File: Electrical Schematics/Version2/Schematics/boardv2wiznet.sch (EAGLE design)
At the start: 19 parts

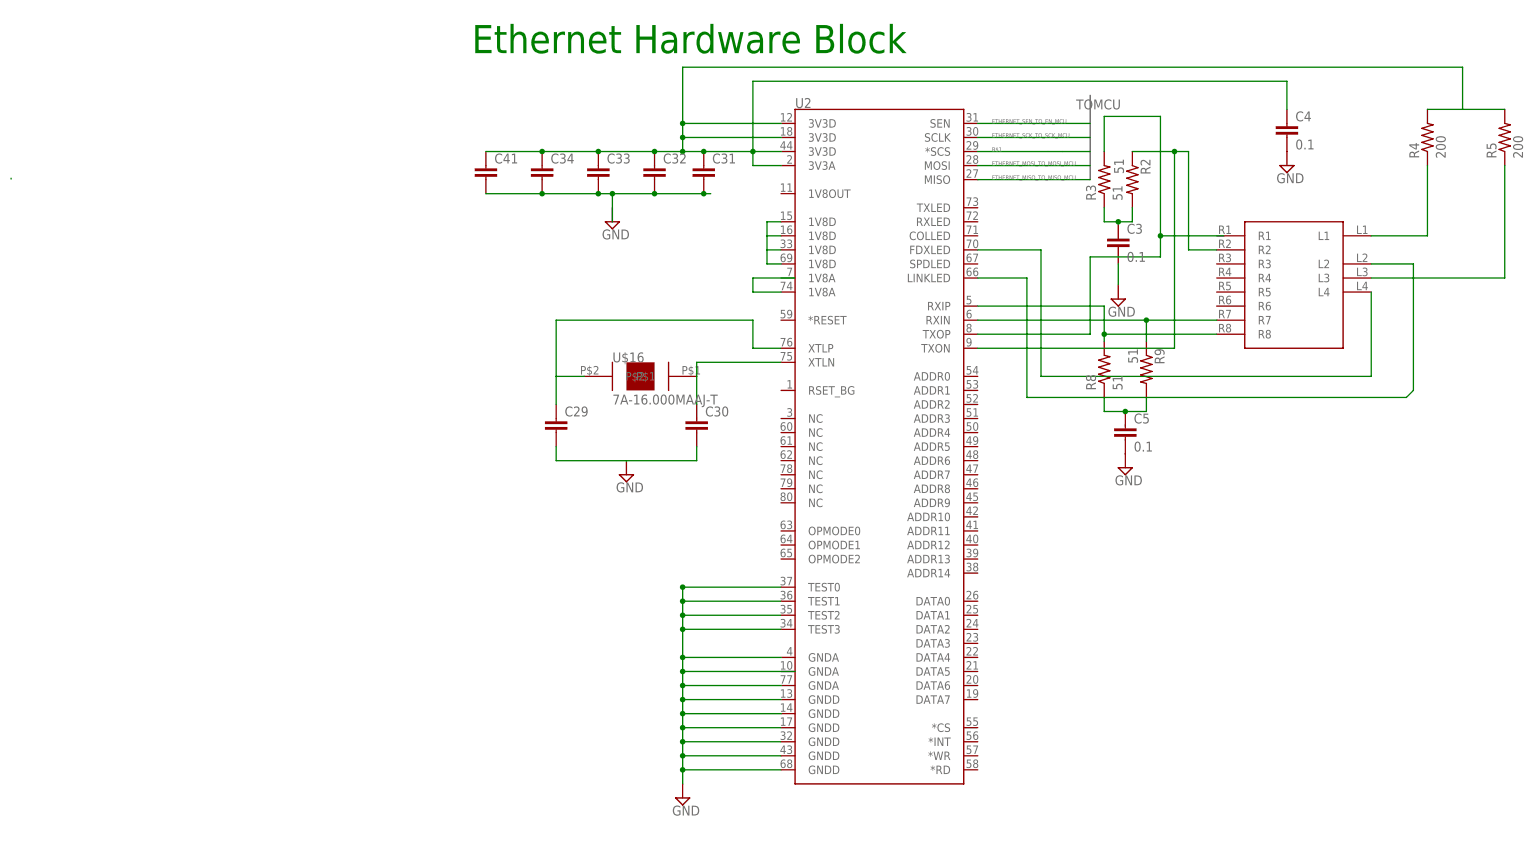
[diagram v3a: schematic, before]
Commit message: updated power and ethernet
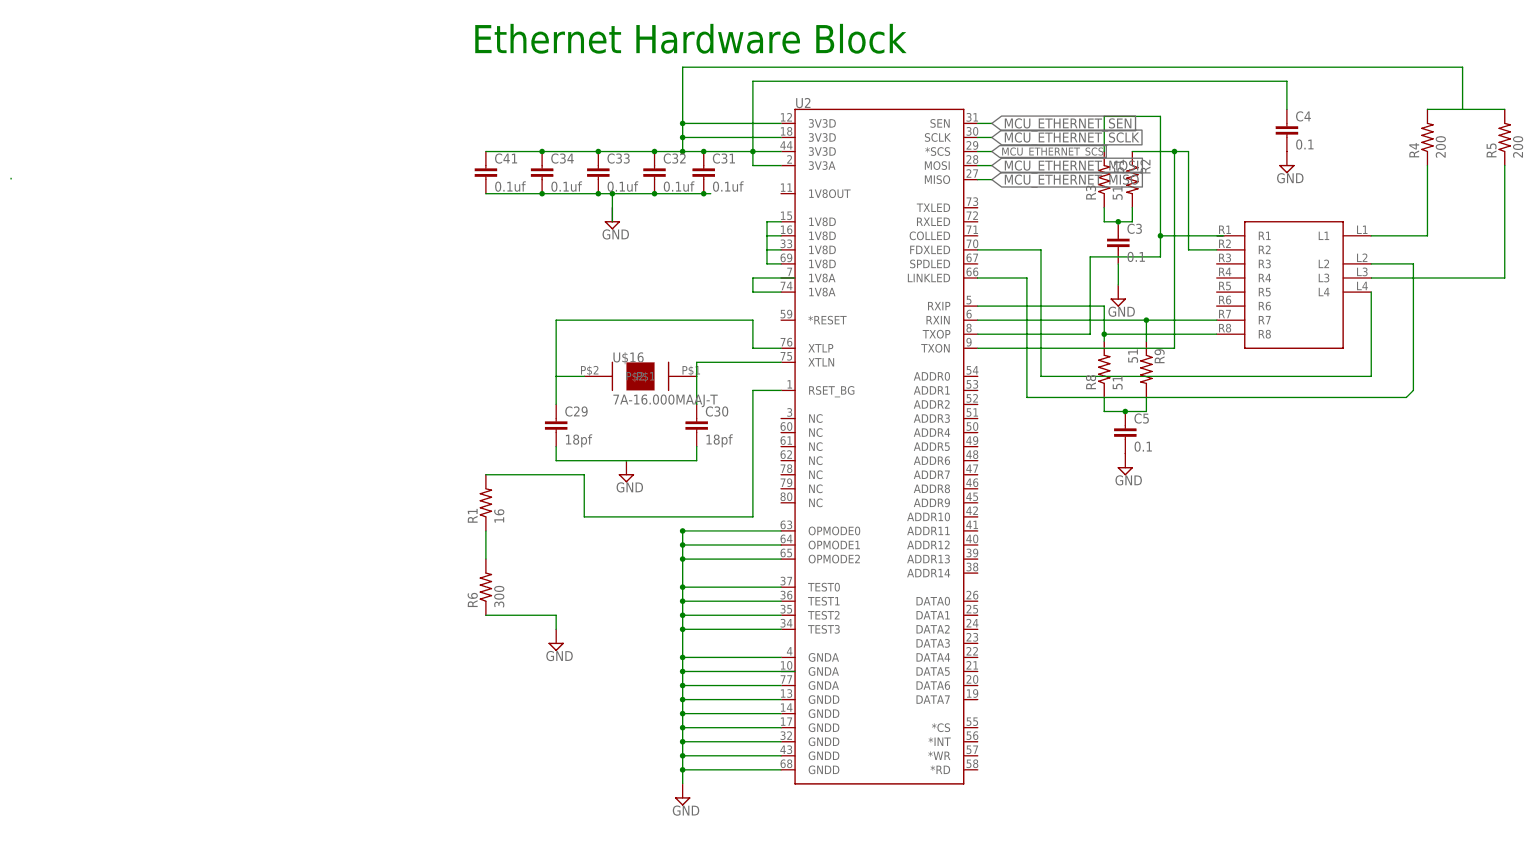
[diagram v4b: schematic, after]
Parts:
- added R1: 16, SparkFun-Passives:RESISTOR0603-RES
- added R6: 300, SparkFun-Passives:RESISTOR0603-RES
- C29, C30: value (none) -> 18pf
- C31, C32, C33, C34, C41: value (none) -> 0.1uf
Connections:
- net B$1 renamed MCU_ETHERNET_SCS
- net ETHERNET_MISO_TO_MISO_MCU renamed MCU_ETHERNET_MISO
- net ETHERNET_MOSI_TO_MOSI_MCU renamed MCU_ETHERNET_MOSI
- net ETHERNET_SCK_TO_SCK_MCU renamed MCU_ETHERNET_SCLK
- net ETHERNET_SEN_TO_EN_MCU renamed MCU_ETHERNET_SEN
- new net N$13: R1.1, R6.2
- new net N$15: R1.2, U2.RSET_BG
- net GND: now also R6.1
- net WIZNET_TO_GND: now also U2.OPMODE0, U2.OPMODE1, U2.OPMODE2
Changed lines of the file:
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@@
 <part name="C5" library="eagle-ltspice" deviceset="C" device="C0603" value="0.1"/>
 <part name="C3" library="eagle-ltspice" deviceset="C" device="C0603" value="0.1"/>
-<part name="C30" library="eagle-ltspice" deviceset="C" device="C0603"/>
-<part name="C29" library="eagle-ltspice" deviceset="C" device="C0603"/>
-<part name="C31" library="eagle-ltspice" deviceset="C" device="C0603"/>
-<part name="C34" library="eagle-ltspice" deviceset="C" device="C0603"/>
+<part name="C30" library="eagle-ltspice" deviceset="C" device="C0603" value="18pf"/>
+<part name="C29" library="eagle-ltspice" deviceset="C" device="C0603" value="18pf"/>
+<part name="C31" library="eagle-ltspice" deviceset="C" device="C0603" value="0.1uf"/>
+<part name="C34" library="eagle-ltspice" deviceset="C" device="C0603" value="0.1uf"/>
 <part name="C4" library="eagle-ltspice" deviceset="C" device="C0603" value="0.1"/>
-<part name="C33" library="eagle-ltspice" deviceset="C" device="C0603"/>
-<part name="C32" library="eagle-ltspice" deviceset="C" device="C0603"/>
-<part name="C41" library="eagle-ltspice" deviceset="C" device="C0603"/>
+<part name="C33" library="eagle-ltspice" deviceset="C" device="C0603" value="0.1uf"/>
+<part name="C32" library="eagle-ltspice" deviceset="C" device="C0603" value="0.1uf"/>
+<part name="C41" library="eagle-ltspice" deviceset="C" device="C0603" value="0.1uf"/>
 <part name="FRAME1" library="frames" deviceset="DOCFIELD" device=""/>
+<part name="R1" library="SparkFun-Passives" deviceset="RESISTOR" device="0603-RES" value="16"/>
+<part name="R6" library="SparkFun-Passives" deviceset="RESISTOR" device="0603-RES" value="300"/>
+<part name="SUPPLY1" library="supply2" deviceset="GND" device=""/>
 </parts>
 <sheets>
@@
 <instance part="C41" gate="G$1" x="-17.78" y="104.14"/>
 <instance part="FRAME1" gate="G$1" x="88.9" y="-12.7"/>
+<instance part="R1" gate="G$1" x="-17.78" y="43.18" rot="R90"/>
+<instance part="R6" gate="G$1" x="-17.78" y="27.94" rot="R90"/>
+<instance part="SUPPLY1" gate="GND" x="-5.08" y="17.78"/>
 </instances>
 <busses>
-<bus name="TOMCU">
-<segment>
-<wire x1="91.44" y1="101.6" x2="91.44" y2="116.84" width="0.762" layer="92"/>
-<label x="88.9" y="114.3" size="1.778" layer="95"/>
-</segment>
-</bus>
 </busses>
 <nets>
@@
 <pinref part="SUPPLY3" gate="GND" pin="GND"/>
 <pinref part="C4" gate="G$1" pin="2"/>
+</segment>
+<segment>
+<pinref part="R6" gate="G$1" pin="1"/>
+<wire x1="-17.78" y1="22.86" x2="-5.08" y2="22.86" width="0.1524" layer="91"/>
+<wire x1="-5.08" y1="22.86" x2="-5.08" y2="20.32" width="0.1524" layer="91"/>
+<pinref part="SUPPLY1" gate="GND" pin="GND"/>
 </segment>
 </net>
@@
 <junction x="17.78" y="25.4"/>
 <junction x="17.78" y="27.94"/>
+<pinref part="U2" gate="G$1" pin="OPMODE0"/>
+<wire x1="35.56" y1="38.1" x2="17.78" y2="38.1" width="0.1524" layer="91"/>
+<wire x1="17.78" y1="38.1" x2="17.78" y2="35.56" width="0.1524" layer="91"/>
+<pinref part="U2" gate="G$1" pin="OPMODE1"/>
+<wire x1="17.78" y1="33.02" x2="17.78" y2="27.94" width="0.1524" layer="91"/>
+<wire x1="35.56" y1="35.56" x2="17.78" y2="35.56" width="0.1524" layer="91"/>
+<wire x1="17.78" y1="35.56" x2="17.78" y2="33.02" width="0.1524" layer="91"/>
+<pinref part="U2" gate="G$1" pin="OPMODE2"/>
+<wire x1="35.56" y1="33.02" x2="17.78" y2="33.02" width="0.1524" layer="91"/>
+<junction x="17.78" y="33.02"/>
+<junction x="17.78" y="35.56"/>
+<junction x="17.78" y="38.1"/>
 </segment>
 </net>
@@
 </segment>
 </net>
-<net name="B$1" class="0">
-<segment>
-<pinref part="U2" gate="G$1" pin="*SCS"/>
-<wire x1="86.36" y1="106.68" x2="83.82" y2="106.68" width="0.1524" layer="91"/>
-<label x="73.66" y="106.68" size="0.762" layer="95"/>
-<wire x1="83.82" y1="106.68" x2="71.12" y2="106.68" width="0.1524" layer="91"/>
-<wire x1="86.36" y1="106.68" x2="91.44" y2="106.68" width="0.1524" layer="91"/>
-</segment>
-</net>
 <net name="N$3" class="0">
 <segment>
@@
 </segment>
 </net>
-<net name="ETHERNET_SEN_TO_EN_MCU" class="0">
+<net name="N$13" class="0">
+<segment>
+<pinref part="R1" gate="G$1" pin="1"/>
+<pinref part="R6" gate="G$1" pin="2"/>
+<wire x1="-17.78" y1="33.02" x2="-17.78" y2="38.1" width="0.1524" layer="91"/>
+</segment>
+</net>
+<net name="N$15" class="0">
+<segment>
+<pinref part="R1" gate="G$1" pin="2"/>
+<wire x1="-17.78" y1="48.26" x2="0" y2="48.26" width="0.1524" layer="91"/>
+<wire x1="0" y1="48.26" x2="0" y2="40.64" width="0.1524" layer="91"/>
+<wire x1="0" y1="40.64" x2="30.48" y2="40.64" width="0.1524" layer="91"/>
+<wire x1="30.48" y1="40.64" x2="30.48" y2="63.5" width="0.1524" layer="91"/>
+<pinref part="U2" gate="G$1" pin="RSET_BG"/>
+<wire x1="30.48" y1="63.5" x2="35.56" y2="63.5" width="0.1524" layer="91"/>
+</segment>
+</net>
+<net name="MCU_ETHERNET_SEN" class="0">
 <segment>
 <pinref part="U2" gate="G$1" pin="SEN"/>
-<wire x1="91.44" y1="111.76" x2="71.12" y2="111.76" width="0.1524" layer="91"/>
-<label x="73.66" y="111.76" size="0.762" layer="95"/>
-</segment>
-</net>
-<net name="ETHERNET_SCK_TO_SCK_MCU" class="0">
+<wire x1="71.12" y1="111.76" x2="73.66" y2="111.76" width="0.1524" layer="91"/>
+<label x="73.66" y="111.76" size="1.778" layer="95" xref="yes"/>
+</segment>
+</net>
+<net name="MCU_ETHERNET_SCLK" class="0">
 <segment>
 <pinref part="U2" gate="G$1" pin="SCLK"/>
-<wire x1="91.44" y1="109.22" x2="71.12" y2="109.22" width="0.1524" layer="91"/>
-<label x="73.66" y="109.22" size="0.762" layer="95"/>
-</segment>
-</net>
-<net name="ETHERNET_MOSI_TO_MOSI_MCU" class="0">
+<wire x1="71.12" y1="109.22" x2="73.66" y2="109.22" width="0.1524" layer="91"/>
+<label x="73.66" y="109.22" size="1.778" layer="95" xref="yes"/>
+</segment>
+</net>
+<net name="MCU_ETHERNET_SCS" class="0">
+<segment>
+<pinref part="U2" gate="G$1" pin="*SCS"/>
+<wire x1="71.12" y1="106.68" x2="73.66" y2="106.68" width="0.1524" layer="91"/>
+<label x="73.66" y="106.68" size="1.4224" layer="95" xref="yes"/>
+</segment>
+</net>
+<net name="MCU_ETHERNET_MOSI" class="0">
 <segment>
 <pinref part="U2" gate="G$1" pin="MOSI"/>
-<wire x1="91.44" y1="104.14" x2="71.12" y2="104.14" width="0.1524" layer="91"/>
-<label x="73.66" y="104.14" size="0.762" layer="95"/>
-</segment>
-</net>
-<net name="ETHERNET_MISO_TO_MISO_MCU" class="0">
+<wire x1="71.12" y1="104.14" x2="73.66" y2="104.14" width="0.1524" layer="91"/>
+<label x="73.66" y="104.14" size="1.778" layer="95" xref="yes"/>
+</segment>
+</net>
+<net name="MCU_ETHERNET_MISO" class="0">
 <segment>
 <pinref part="U2" gate="G$1" pin="MISO"/>
-<wire x1="91.44" y1="101.6" x2="71.12" y2="101.6" width="0.1524" layer="91"/>
-<label x="73.66" y="101.6" size="0.762" layer="95"/>
-</segment>
-</net>
+<wire x1="71.12" y1="101.6" x2="73.66" y2="101.6" width="0.1524" layer="91"/>
+<label x="73.66" y="101.6" size="1.778" layer="95" xref="yes"/>
+</segment>
+</net>
